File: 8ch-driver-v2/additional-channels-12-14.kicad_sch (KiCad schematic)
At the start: 42 parts, among them Q3 2N7002E, Q4 2N7002E, Q5 2N7002E, U3 DRV104PWP, U4 DRV104PWP, U5 DRV104PWP

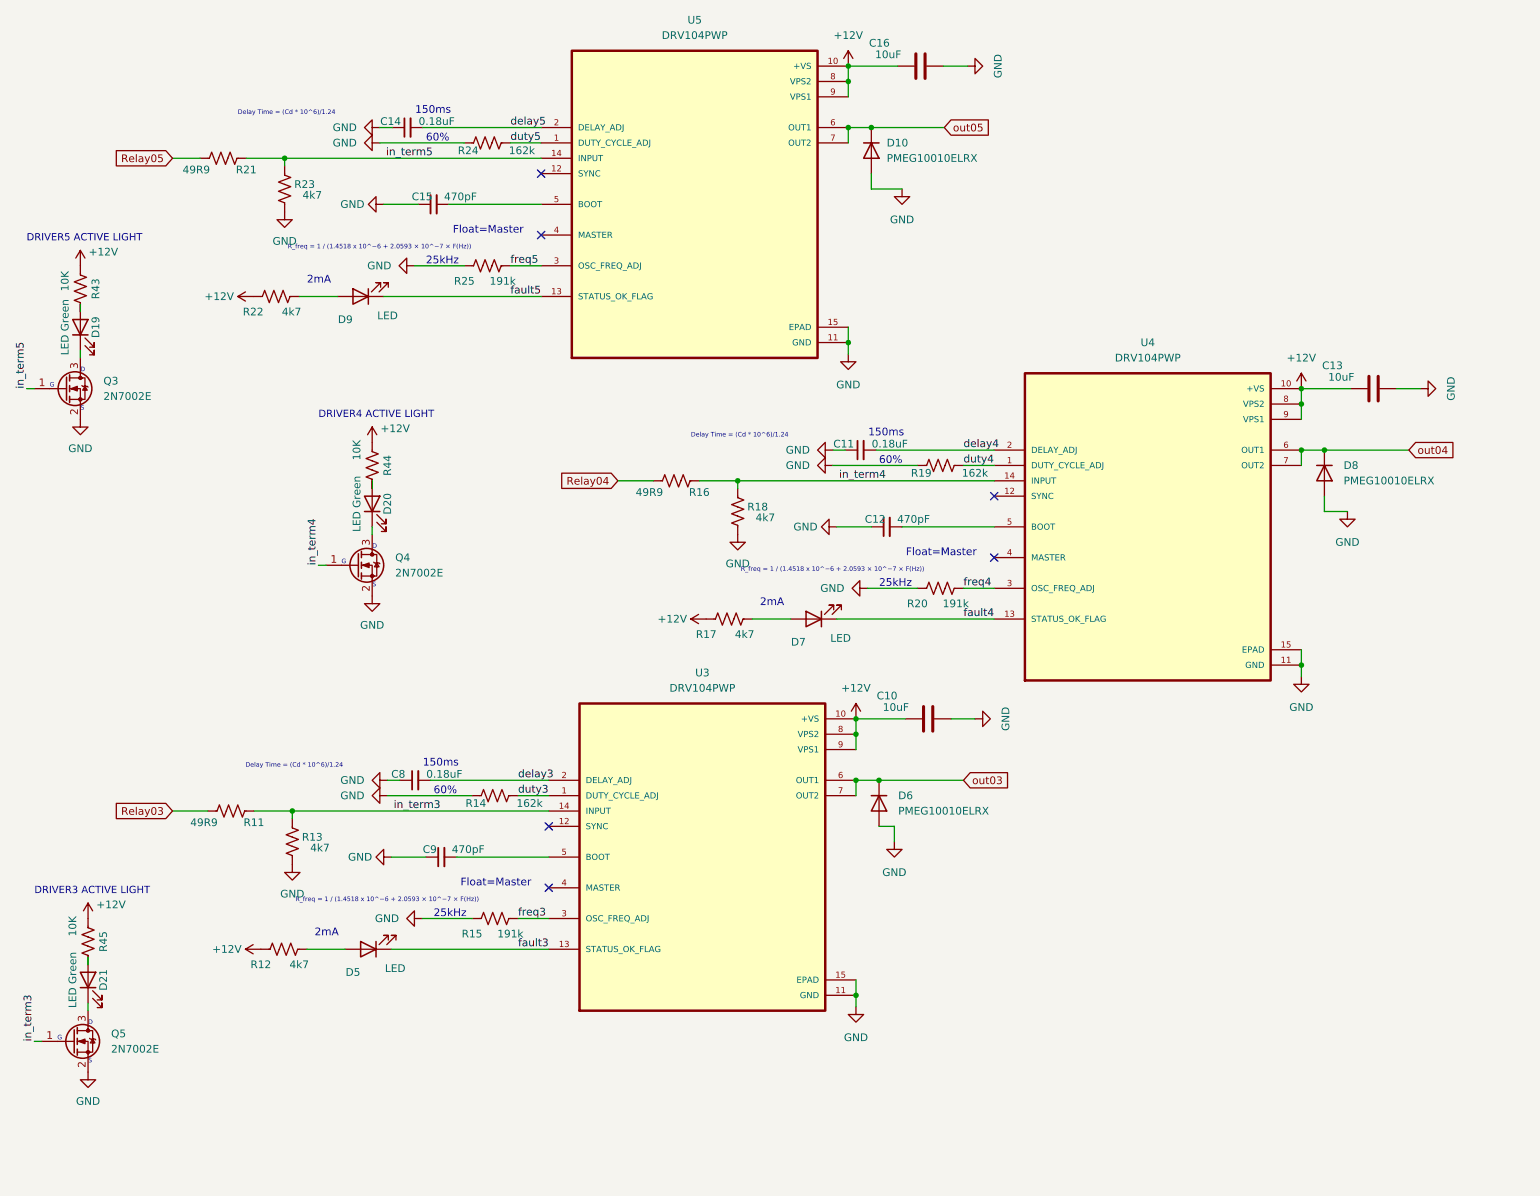
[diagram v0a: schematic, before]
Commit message: added 8 more channels and an FTDH chip
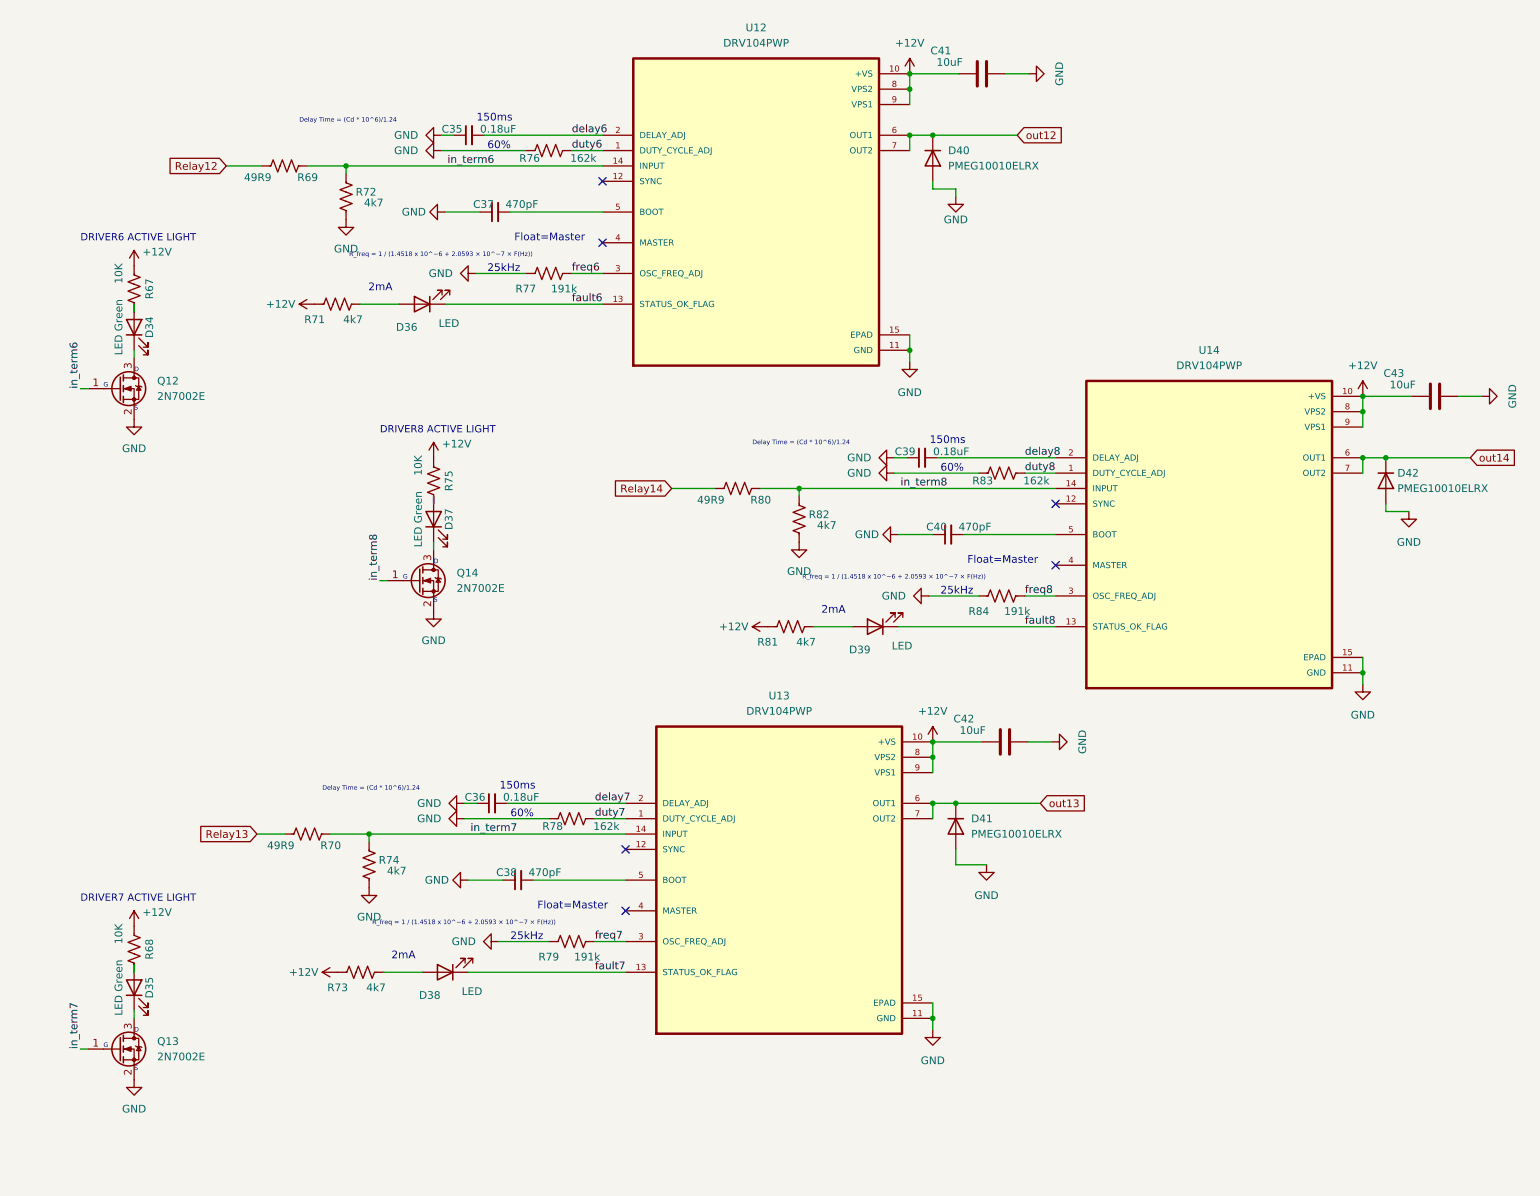
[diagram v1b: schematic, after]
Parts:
- removed C10, C13, C16: 10uF, Capacitor_SMD:C_1210_3225Metric, symbol Device:C
- removed C11, C14, C8: 0.18uF, Capacitor_SMD:C_1206_3216Metric, symbol Device:C_Small
- removed C12, C15, C9: 470pF, Capacitor_SMD:C_1206_3216Metric, symbol Device:C_Small
- removed D10, D6, D8: PMEG10010ELRX, Diode_SMD:Nexperia_CFP3_SOD-123W, symbol Device:D
- removed D19, D20, D21: LED Green, LED_SMD:LED_0805_2012Metric, symbol Device:LED
- removed D5, D7, D9: LED, LED_SMD:LED_0805_2012Metric, symbol Device:LED
- removed Q3, Q4, Q5: 2N7002E, Package_TO_SOT_SMD:SOT-23, symbol Transistor_FET:2N7002E
- removed R11, R16, R21: 49R9, Resistor_SMD:R_1206_3216Metric, symbol Device:R_US
- removed R12, R13, R17, R18, R22, R23: 4k7, Resistor_SMD:R_1206_3216Metric, symbol Device:R_US
- removed R14, R19, R24: 162k, Resistor_SMD:R_1206_3216Metric, symbol Device:R_US
- removed R15, R20, R25: 191k, Resistor_SMD:R_1206_3216Metric, symbol Device:R_US
- removed R43, R44, R45: 10K, Resistor_SMD:R_1206_3216Metric, symbol Device:R_US
- removed U3, U4, U5: DRV104PWP, Solenoid_Driver:IC_TPS27S100BPWPR, symbol DRV104PWP:DRV104PWP
- added C35, C36, C39: 0.18uF, Capacitor_SMD:C_1206_3216Metric, symbol Device:C_Small
- added C37, C38, C40: 470pF, Capacitor_SMD:C_1206_3216Metric, symbol Device:C_Small
- added C41, C42, C43: 10uF, Capacitor_SMD:C_1210_3225Metric, symbol Device:C
- added D34, D35, D37: LED Green, LED_SMD:LED_0805_2012Metric, symbol Device:LED
- added D36, D38, D39: LED, LED_SMD:LED_0805_2012Metric, symbol Device:LED
- added D40, D41, D42: PMEG10010ELRX, Diode_SMD:Nexperia_CFP3_SOD-123W, symbol Device:D
- added Q12, Q13, Q14: 2N7002E, Package_TO_SOT_SMD:SOT-23, symbol Transistor_FET:2N7002E
- added R67, R68, R75: 10K, Resistor_SMD:R_1206_3216Metric, symbol Device:R_US
- added R69, R70, R80: 49R9, Resistor_SMD:R_1206_3216Metric, symbol Device:R_US
- added R71, R72, R73, R74, R81, R82: 4k7, Resistor_SMD:R_1206_3216Metric, symbol Device:R_US
- added R76, R78, R83: 162k, Resistor_SMD:R_1206_3216Metric, symbol Device:R_US
- added R77, R79, R84: 191k, Resistor_SMD:R_1206_3216Metric, symbol Device:R_US
- added U12, U13, U14: DRV104PWP, Solenoid_Driver:IC_TPS27S100BPWPR, symbol DRV104PWP:DRV104PWP
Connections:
- net +12V: now also C41.1, C42.1, C43.1, R67.1, R68.1, R71.1, R73.1, R75.1, R81.1, U12.10 (+VS), U12.8 (VPS2), U12.9 (VPS1), U13.10 (+VS), U13.8 (VPS2), U13.9 (VPS1), U14.10 (+VS), U14.8 (VPS2), U14.9 (VPS1)
- net GND: now also C35.1, C36.1, C37.1, C38.1, C39.1, C40.1, C41.2, C42.2, C43.2, D40.2 (A), D41.2 (A), D42.2 (A), Q12.2 (S), Q13.2 (S), Q14.2 (S), R72.1, R74.1, R76.1, R77.1, R78.1, R79.1, R82.1, R83.1, R84.1, U12.11 (GND), U12.15 (EPAD), U13.11 (GND), U13.15 (EPAD), U14.11 (GND), U14.15 (EPAD)
- new net: D34.1 (K), Q12.3 (D)
- new net: D36.2 (A), R71.2
- new net: D34.2 (A), R67.2
- new net: C40.2, U14.5 (BOOT)
- new net: D37.2 (A), R75.2
- new net: D37.1 (K), Q14.3 (D)
- new net: C38.2, U13.5 (BOOT)
- new net: D39.2 (A), R81.2
- new net: D38.2 (A), R73.2
- new net: C37.2, U12.5 (BOOT)
- new net: D35.1 (K), Q13.3 (D)
- new net: D35.2 (A), R68.2
- new net Relay12: R69.1
- new net Relay13: R70.1
- new net Relay14: R80.1
- new net delay6: C35.2, U12.2 (DELAY_ADJ)
- new net delay7: C36.2, U13.2 (DELAY_ADJ)
- new net delay8: C39.2, U14.2 (DELAY_ADJ)
- new net duty6: R76.2, U12.1 (DUTY_CYCLE_ADJ)
- new net duty7: R78.2, U13.1 (DUTY_CYCLE_ADJ)
- new net duty8: R83.2, U14.1 (DUTY_CYCLE_ADJ)
- new net fault6: D36.1 (K), U12.13 (STATUS_OK_FLAG)
- new net fault7: D38.1 (K), U13.13 (STATUS_OK_FLAG)
- new net fault8: D39.1 (K), U14.13 (STATUS_OK_FLAG)
- new net freq6: R77.2, U12.3 (OSC_FREQ_ADJ)
- new net freq7: R79.2, U13.3 (OSC_FREQ_ADJ)
- new net freq8: R84.2, U14.3 (OSC_FREQ_ADJ)
- new net in_term6: Q12.1 (G), R69.2, R72.2, U12.14 (INPUT)
- new net in_term7: Q13.1 (G), R70.2, R74.2, U13.14 (INPUT)
- new net in_term8: Q14.1 (G), R80.2, R82.2, U14.14 (INPUT)
- new net out12: D40.1 (K), U12.6 (OUT1), U12.7 (OUT2)
- new net out13: D41.1 (K), U13.6 (OUT1), U13.7 (OUT2)
- new net out14: D42.1 (K), U14.6 (OUT1), U14.7 (OUT2)
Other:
- note added: "DRIVER6 ACTIVE LIGHT"
- note added: "DRIVER7 ACTIVE LIGHT"
- note added: "DRIVER8 ACTIVE LIGHT"
- note removed: "DRIVER3 ACTIVE LIGHT"
- note removed: "DRIVER4 ACTIVE LIGHT"
- note removed: "DRIVER5 ACTIVE LIGHT"
- company: Boston University -> (none)

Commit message: mucho mas progresso
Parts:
- removed C35: 0.18uF, Capacitor_SMD:C_1206_3216Metric, symbol Device:C_Small
- removed C38: 470pF, Capacitor_SMD:C_1206_3216Metric, symbol Device:C_Small
- removed C42, C43: 10uF, Capacitor_SMD:C_1210_3225Metric, symbol Device:C
- removed D34, D37: LED Green, LED_SMD:LED_0805_2012Metric, symbol Device:LED
- removed D41, D42: PMEG10010ELRX, Diode_SMD:Nexperia_CFP3_SOD-123W, symbol Device:D
- added C35, C38: 10uF, Capacitor_SMD:C_1210_3225Metric, symbol Device:C
- added C42: 0.18uF, Capacitor_SMD:C_1206_3216Metric, symbol Device:C_Small
- added C43: 470pF, Capacitor_SMD:C_1206_3216Metric, symbol Device:C_Small
- added D34, D37: PMEG10010ELRX, Diode_SMD:Nexperia_CFP3_SOD-123W, symbol Device:D
- added D41: LED Green, LED_SMD:LED_0805_2012Metric, symbol Device:LED
- added D42: LED, LED_SMD:LED_0805_2012Metric, symbol Device:LED
- D38: value LED -> LED Green
- R68: value 10K -> 162k
- R70: value 49R9 -> 4k7; PartNum RC0805FR-0749R9L -> RC0805JR-074K7L
- R71: value 4k7 -> 191k; PartNum RC0805JR-074K7L -> RC0805FR-07191KL
- R73: value 4k7 -> 10K; PartNum RC0805JR-074K7L -> RC0805FR-07162KL
- R74: value 4k7 -> 162k; PartNum RC0805JR-074K7L -> RC0805FR-07162KL
- R75: value 10K -> 49R9; PartNum RC0805FR-07162KL -> RC0805FR-0749R9L
- R76, R78: value 162k -> 4k7; PartNum RC0805FR-07162KL -> RC0805JR-074K7L
- R79: value 191k -> 10K; PartNum RC0805FR-07191KL -> RC0805FR-07162KL
- R80: value 49R9 -> 162k; PartNum RC0805FR-0749R9L -> RC0805FR-07162KL
- R81: value 4k7 -> 49R9; PartNum RC0805JR-074K7L -> RC0805FR-0749R9L
- R83: value 162k -> 191k; PartNum RC0805FR-07162KL -> RC0805FR-07191KL
- R84: value 191k -> 4k7; PartNum RC0805FR-07191KL -> RC0805JR-074K7L
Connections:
- net +12V: now also R72.1, R78.1, R79.1, R84.1, C35.1, C38.1; no longer R68.1, R71.1, R75.1, R81.1
- net GND: now also R68.1, R70.1, R71.1, R80.1, C35.2, C38.2, C42.1, C43.1, D34.2 (A), D37.2 (A); no longer R72.1, R78.1, R79.1, R84.1
- net Relay13: now also R75.1; no longer R70.1
- net Relay14: now also R81.1; no longer R80.1
- net out12: now also D34.1 (K); no longer D40.1 (K)
- net out13: now also D37.1 (K)
- net out14: now also D40.1 (K)
- net at Q12.3 (D): now also D35.1 (K)
- net at D36.2 (A): now also R72.2; no longer R71.2
- net at R67.2: now also D35.2 (A)
- net at C40.2: now also U13.5 (BOOT); no longer U14.5 (BOOT)
- net in_term13: now reaches R75.2
- net in_term13: now also Q13.1 (G), R76.2, U13.14 (INPUT)
- net at Q14.3 (D): now also D41.1 (K)
- net at D39.2 (A): now also R78.2; no longer R81.2
- net at Q13.3 (D): now also D38.1 (K); no longer D35.1 (K)
- net duty12: now reaches R68.2
- net duty12: now also U12.1 (DUTY_CYCLE_ADJ); no longer D35.2 (A)
- net delay6 renamed delay12
- net delay12: now also C36.2
- net delay7 renamed delay13
- net delay13: now also C39.2; no longer C36.2
- net delay8 renamed delay14
- net delay14: now also C42.2; no longer C39.2
- removed net duty6: R76.2, U12.1 (DUTY_CYCLE_ADJ)
- net duty7 renamed duty13\
- net duty13\: now also R74.2; no longer R78.2
- net duty8 renamed duty14
- net duty14: now also R80.2; no longer R83.2
- net fault6 renamed fault12
- net fault7 renamed fault13
- net fault13: now also D39.1 (K); no longer D38.1 (K)
- net fault8 renamed fault14
- net fault14: now also D42.1 (K); no longer D39.1 (K)
- net freq6 renamed freq12
- net freq12: now also R71.2; no longer R77.2
- net freq7: no longer names the net of R79.2
- net freq7: now also D41.2 (A); no longer U13.3 (OSC_FREQ_ADJ)
- net freq8: no longer names the net of R84.2
- net freq8: now also D42.2 (A); no longer U14.3 (OSC_FREQ_ADJ)
- net in_term6 renamed in_term12
- net in_term12: now also R70.2; no longer R72.2
- removed net in_term7: Q13.1 (G), R70.2, R74.2, U13.14 (INPUT)
- net in_term8 renamed in_term14
- net in_term14: now also R81.2; no longer R80.2
- new net: C43.2, U14.5 (BOOT)
- new net freq13: R77.2, U13.3 (OSC_FREQ_ADJ)
- new net freq14: R83.2, U14.3 (OSC_FREQ_ADJ)
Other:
- note removed: "DRIVER7 ACTIVE LIGHT"
- note removed: "DRIVER8 ACTIVE LIGHT"
